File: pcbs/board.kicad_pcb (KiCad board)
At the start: 2 copper layers, 120.3 x 95.9 mm, 68 parts

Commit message: chore: release v0.2
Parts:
- removed the REF** at (72.6, 8.63)
- removed the REF** at (37.9, -55.9)
- removed the REF** at (75.9, -12.5)
- removed the REF** at (56.9, -49.9)
- removed the REF** at (56.9, -32.9)
- removed the REF** at (18.9, -17.6)
- removed the REF** at (47.4, 5.30)
- removed the REF** at (37.9, -38.9)
- removed the REF** at (37.9, -21.9)
- removed the REF** at (18.9, -34.6)
- removed the REF** at (75.9, -29.5)
- removed the REF** at (56.9, -15.9)
- removed the REF** at (18.9, -51.6)
- removed the REF** at (75.9, -46.5)
- removed the REF** at (108.6, -10.0)
- removed the REF** at (107.1, -10.0)
- removed the REF** at (-0.15, -40.6)
- removed the REF** at (86.9, 17.4)
- added REF**: VIA-0.6mm, VIA-0.6mm, F.Cu at (18.6, -17.0)
- added REF**: VIA-0.6mm, VIA-0.6mm, F.Cu at (18.6, -34.0)
- added REF**: VIA-0.6mm, VIA-0.6mm, F.Cu at (37.6, -38.2)
- added REF**: VIA-0.6mm, VIA-0.6mm, F.Cu at (75.6, -45.9)
- added REF**: VIA-0.6mm, VIA-0.6mm, F.Cu at (56.6, -49.3)
- added REF**: VIA-0.6mm, VIA-0.6mm, F.Cu at (75.1, 11.0)
- added REF**: VIA-0.6mm, VIA-0.6mm, F.Cu at (56.6, -15.3)
- added REF**: VIA-0.6mm, VIA-0.6mm, F.Cu at (107.2, -7.90)
- added REF**: VIA-0.6mm, VIA-0.6mm, F.Cu at (-0.39, -39.9)
- added REF**: VIA-0.6mm, VIA-0.6mm, F.Cu at (53.1, 8.09)
- added REF**: VIA-0.6mm, VIA-0.6mm, F.Cu at (56.6, -32.3)
- added REF**: VIA-0.6mm, VIA-0.6mm, F.Cu at (75.6, -11.9)
- added REF**: VIA-0.6mm, VIA-0.6mm, F.Cu at (18.6, -51.0)
- added REF**: VIA-0.6mm, VIA-0.6mm, F.Cu at (37.6, -21.2)
- added REF**: VIA-0.6mm, VIA-0.6mm, F.Cu at (75.6, -28.9)
- added REF**: VIA-0.6mm, VIA-0.6mm, F.Cu at (37.6, -55.2)
- added REF**: VIA-0.6mm, VIA-0.6mm, F.Cu at (87.1, 18.1)
- added REF**: VIA-0.6mm, VIA-0.6mm, F.Cu at (105.7, -7.90)
- moved D16 50.8 mm to (98.9, 23.7), turned to -120 degrees
- moved D18 45.1 mm to (54.1, 21.1), turned to 180 degrees
- moved S16 26.1 mm to (73.0, 18.7), turned to -15 degrees
- moved S17 17.3 mm to (53.1, 16.1), turned to 0 degrees
- moved H5 4.54 mm to (86.2, 11.7)
- moved SW2 3.44 mm to (106.4, 1.60)
- moved D17 3.19 mm to (72.7, 23.8)
- moved ? 2.96 mm to (93.2, 1.60)
- moved ICON1 2.96 mm to (93.2, 1.60)
- moved JST1 2.74 mm to (101.2, 1.60)
- moved SW1 2.56 mm to (106.5, -7.90)
- moved H6 2.25 mm to (105.2, 9.42), turned to 30 degrees
- moved H7 2.24 mm to (87.6, -0.72), turned to -60 degrees
- moved MCU1 1.60 mm to (96.4, -29.9)
- moved DISP1 1.60 mm to (96.4, -25.9)
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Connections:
- D16 pad 2: near_thumb -> far_thumb
- D18 pad 2: far_thumb -> near_thumb
- S16 pad 1: near_thumb -> home_thumb
- S16 pad 2: col_middle -> col_index
- S17 pad 1: home_thumb -> near_thumb
- S17 pad 2: col_index -> col_middle
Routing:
- net row_top: track 131.1 -> 110.8 mm
- net row_home: track 131.3 -> 111.2 mm
- net row_bottom: track 145.4 -> 125.8 mm
- net row_thumb: track 133.8 -> 115.8 mm
- net GND: track 98.8 -> 116.4 mm, vias 1 -> 0
- net col_inner: track 211.6 -> 202.0 mm
- net RAW: track 59.1 -> 63.9 mm
- net col_middle: track 223.6 -> 219.5 mm
- net inner_home: track 28.0 -> 24.0 mm
- net ring_top: track 28.0 -> 24.0 mm
- net far_thumb: track 28.0 -> 24.0 mm
- net index_bottom: track 28.0 -> 24.0 mm
- net index_home: track 28.0 -> 24.0 mm
- net home_thumb: track 28.0 -> 24.0 mm
- net middle_home: track 28.0 -> 24.0 mm
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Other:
- board size 120.3 x 95.9 mm -> 118.6 x 93.2 mm
- board text added: "JLCJLCJLCJLC"
- board text added: "OFF"
- board text added: "ON"
- board text added: "korne v0.2 by Xuyuan Pang"
- board text removed: "korne v0.1 by Xuyuan Pang"

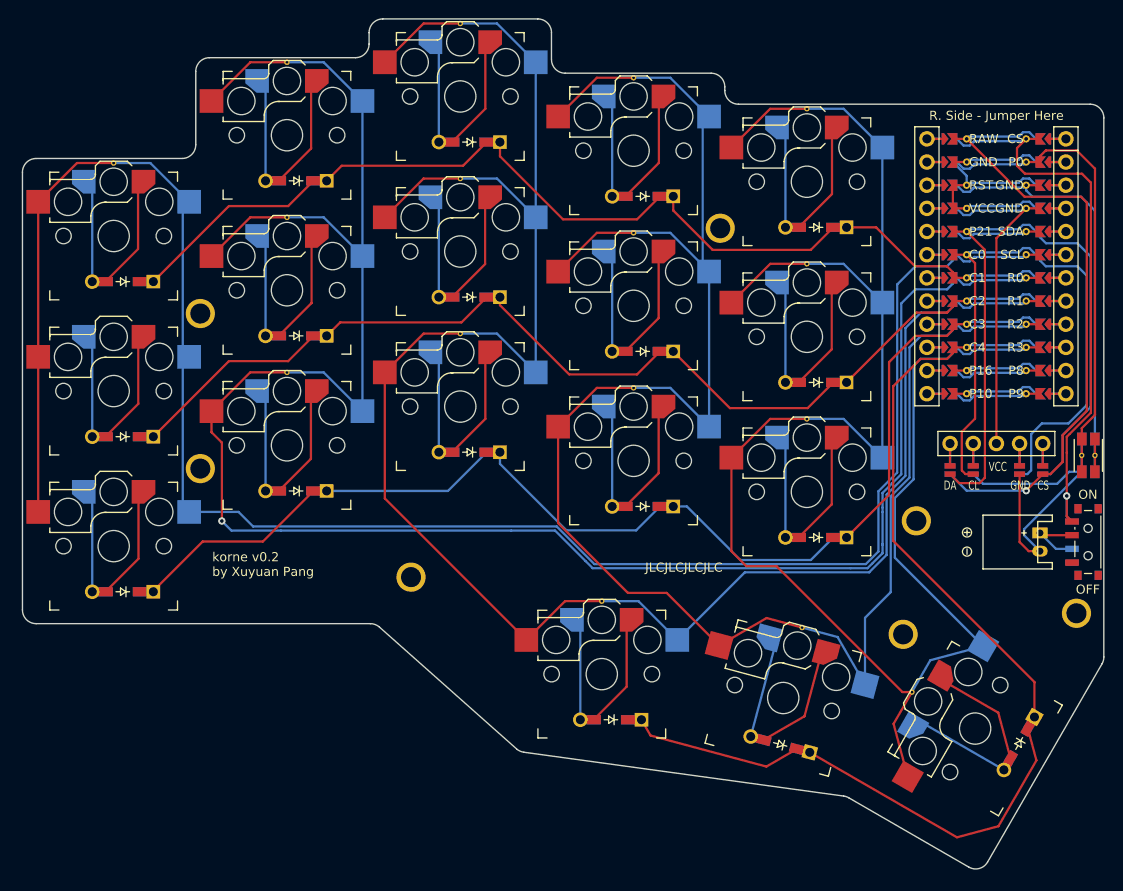
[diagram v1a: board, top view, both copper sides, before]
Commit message: feat(pcbs): added routed v0.3 pcb
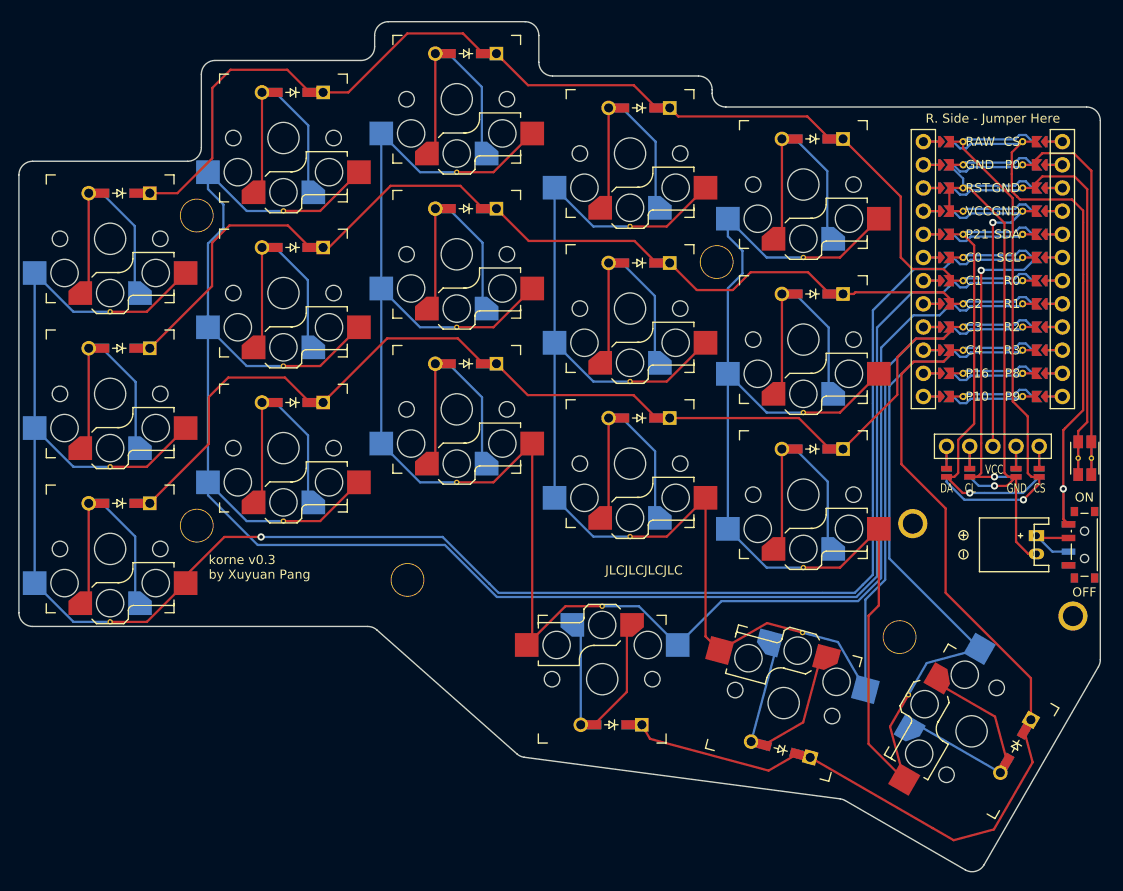
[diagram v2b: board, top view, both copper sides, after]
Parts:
- removed the REF** at (18.6, -17.0)
- removed the REF** at (18.6, -34.0)
- removed the REF** at (37.6, -38.2)
- removed the REF** at (75.6, -45.9)
- removed the REF** at (56.6, -49.3)
- removed the REF** at (75.1, 11.0)
- removed the REF** at (56.6, -15.3)
- removed the REF** at (107.2, -7.90)
- removed the REF** at (-0.39, -39.9)
- removed the REF** at (53.1, 8.09)
- removed the REF** at (56.6, -32.3)
- removed the REF** at (75.6, -11.9)
- removed the REF** at (18.6, -51.0)
- removed the REF** at (37.6, -21.2)
- removed the REF** at (75.6, -28.9)
- removed the REF** at (37.6, -55.2)
- removed the REF** at (87.1, 18.1)
- removed the REF** at (105.7, -7.90)
- added REF**: VIA-0.6mm, VIA-0.6mm, F.Cu at (37.2, -38.9)
- added REF**: VIA-0.6mm, VIA-0.6mm, F.Cu at (37.2, -4.94)
- added REF**: VIA-0.6mm, VIA-0.6mm, F.Cu at (75.1, 11.5)
- added REF**: VIA-0.6mm, VIA-0.6mm, F.Cu at (75.2, -12.6)
- added REF**: VIA-0.6mm, VIA-0.6mm, F.Cu at (106.8, -7.59)
- added REF**: VIA-0.6mm, VIA-0.6mm, F.Cu at (-0.77, -23.6)
- added REF**: VIA-0.6mm, VIA-0.6mm, F.Cu at (18.2, -17.7)
- added REF**: VIA-0.6mm, VIA-0.6mm, F.Cu at (56.2, -16.0)
- added REF**: VIA-0.6mm, VIA-0.6mm, F.Cu at (53.2, 8.64)
- added REF**: VIA-0.6mm, VIA-0.6mm, F.Cu at (56.2, -33.0)
- added REF**: VIA-0.6mm, VIA-0.6mm, F.Cu at (75.2, 4.41)
- added REF**: VIA-0.6mm, VIA-0.6mm, F.Cu at (-0.77, 10.4)
- added REF**: VIA-0.6mm, VIA-0.6mm, F.Cu at (18.2, -0.69)
- added REF**: VIA-0.6mm, VIA-0.6mm, F.Cu at (37.2, -21.9)
- added REF**: VIA-0.6mm, VIA-0.6mm, F.Cu at (75.2, -29.6)
- added REF**: VIA-0.6mm, VIA-0.6mm, F.Cu at (105.4, -7.59)
- added REF**: VIA-0.6mm, VIA-0.6mm, F.Cu at (56.2, 1.01)
- added REF**: VIA-0.6mm, VIA-0.6mm, F.Cu at (18.2, -34.7)
- added REF**: VIA-0.6mm, VIA-0.6mm, F.Cu at (86.7, 18.4)
- added REF**: VIA-0.6mm, VIA-0.6mm, F.Cu at (-0.77, -6.64)
- moved H1 10.8 mm to (8.73, -34.2)
- moved D9 9.70 mm to (38.2, -51.9)
- moved D1 9.70 mm to (0.23, -2.64)
- moved D10 9.70 mm to (57.2, -12.0)
- moved D8 9.70 mm to (38.2, -34.9)
- moved D14 9.70 mm to (76.2, -25.6)
- moved D15 9.70 mm to (76.2, -42.6)
- moved D7 9.70 mm to (38.2, -17.9)
- moved D4 9.70 mm to (19.2, -13.7)
- moved D12 9.70 mm to (57.2, -46.0)
- moved D2 9.70 mm to (0.23, -19.6)
- moved D5 9.70 mm to (19.2, -30.7)
- moved D11 9.70 mm to (57.2, -29.0)
- moved D6 9.70 mm to (19.2, -47.7)
- moved D13 9.70 mm to (76.2, -8.59)
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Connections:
- SW1 pad 1: GND -> RST
- SW1 pad 2: RST -> GND
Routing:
- net MOSI: track 76.0 -> 50.6 mm, vias 0 -> 1
- net SCK: track 69.7 -> 45.5 mm, vias 0 -> 2
- net col_index: track 204.0 -> 187.1 mm
- net GND: track 116.4 -> 131.6 mm, vias 0 -> 1
- net col_middle: track 219.5 -> 207.0 mm
- net row_top: track 110.8 -> 121.3 mm
- net col_pinky: track 215.9 -> 225.8 mm, vias 0 -> 1
- net row_bottom: track 125.8 -> 118.2 mm
- net CS: track 70.2 -> 63.9 mm
- net col_inner: track 202.0 -> 196.8 mm
- net col_ring: track 227.6 -> 223.8 mm, vias 1 -> 0
- net row_thumb: track 115.8 -> 114.3 mm
- net VCC: track 37.3 -> 38.5 mm, vias 0 -> 1
- net RST: track 51.4 -> 52.5 mm
- net RAW: track 63.9 -> 64.4 mm
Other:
- outline, holes or cut-outs redrawn
- board text added: "korne v0.3 by Xuyuan Pang"
- board text removed: "korne v0.2 by Xuyuan Pang"

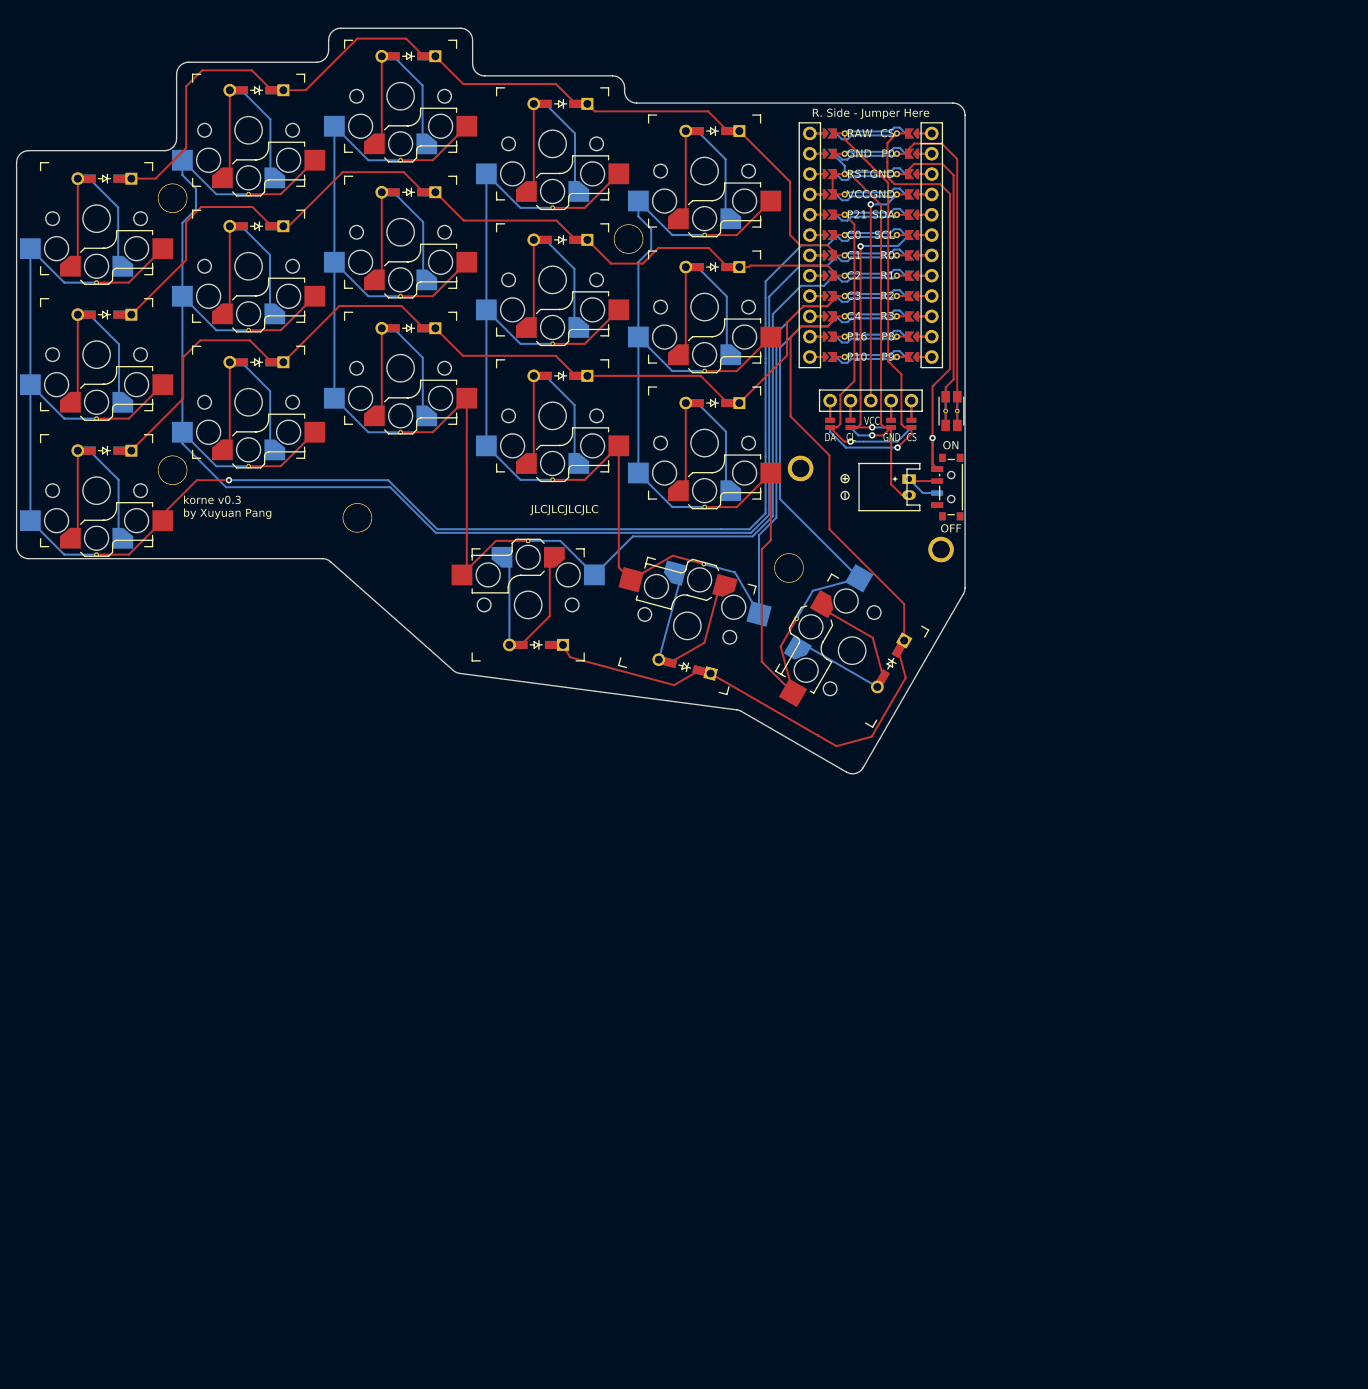
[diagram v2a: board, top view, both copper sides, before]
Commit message: feat(pcbs): adjust traces & updated preview images
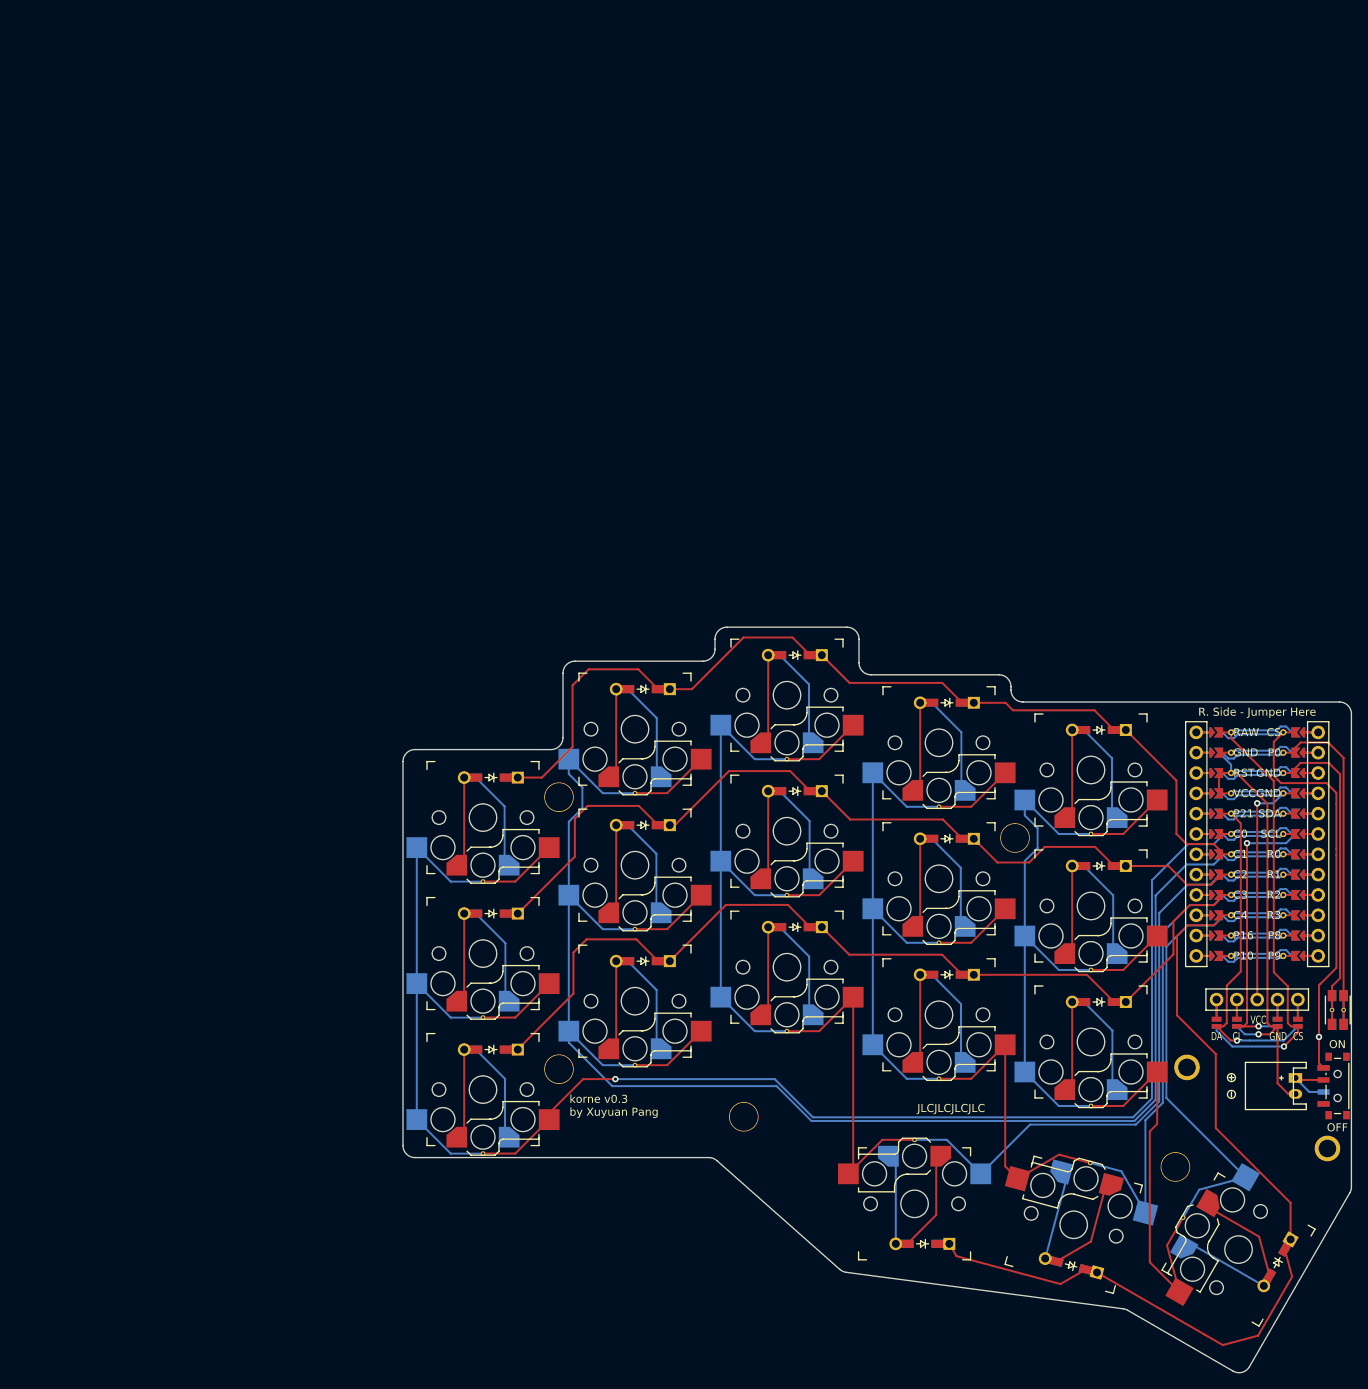
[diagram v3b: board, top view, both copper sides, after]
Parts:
- moved REF** 89.1 mm to (123.4, 86.4)
- moved ? 89.1 mm to (141.1, 76.8)
- moved D1 89.1 mm to (48.5, 72.2)
- moved D10 89.1 mm to (105.5, 62.9)
- moved D11 89.1 mm to (105.5, 45.9)
- moved D12 89.1 mm to (105.5, 28.9)
- moved D13 89.1 mm to (124.5, 66.3)
- moved D14 89.1 mm to (124.5, 49.3)
- moved D15 89.1 mm to (124.5, 32.3)
- moved D16 89.1 mm to (146.8, 98.9)
- moved D17 89.1 mm to (121.0, 99.2)
- moved D18 89.1 mm to (102.5, 96.5)
- moved D2 89.1 mm to (48.5, 55.2)
- moved D3 89.1 mm to (48.5, 38.2)
- moved D4 89.1 mm to (67.5, 61.2)
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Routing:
- net col_pinky: track 225.8 -> 223.7 mm
- net col_ring: track 223.8 -> 221.7 mm
- net col_middle: track 207.0 -> 205.9 mm
- net row_home: track 111.7 -> 112.4 mm
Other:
- outline, holes or cut-outs redrawn
